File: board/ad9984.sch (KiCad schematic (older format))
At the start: 29 parts, among them P401 AD9984 I2C, U401 AD9984

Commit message: Use smaller testpoint pad
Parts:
- TP401, TP402, TP403, TP404: footprint SMD_Packages:1Pin -> 2MM-TESTPOINT:2MM-TESTPOINT
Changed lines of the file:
@@
 F 0 "TP402" V 6200 5300 60  0000 C CNN
 F 1 "TESTPOINT" H 6150 5300 60  0001 C CNN
-F 2 "SMD_Packages:1Pin" H 6150 5350 60  0001 C CNN
+F 2 "2MM-TESTPOINT:2MM-TESTPOINT" H 6150 5350 60  0001 C CNN
 F 3 "" H 6150 5350 60  0000 C CNN
 	1    6150 5350
@@
 F 0 "TP401" V 4300 4600 60  0000 C CNN
 F 1 "TESTPOINT" H 4400 4400 60  0001 C CNN
-F 2 "SMD_Packages:1Pin" H 4400 4450 60  0001 C CNN
+F 2 "2MM-TESTPOINT:2MM-TESTPOINT" H 4400 4450 60  0001 C CNN
 F 3 "" H 4400 4450 60  0000 C CNN
 	1    4400 4450
@@
 F 0 "TP404" V 6850 1900 60  0000 C CNN
 F 1 "TESTPOINT" H 6950 1700 60  0001 C CNN
-F 2 "SMD_Packages:1Pin" H 6950 1750 60  0001 C CNN
+F 2 "2MM-TESTPOINT:2MM-TESTPOINT" H 6950 1750 60  0001 C CNN
 F 3 "" H 6950 1750 60  0000 C CNN
 	1    6950 1750
@@
 F 0 "TP403" V 6950 1900 60  0000 C CNN
 F 1 "TESTPOINT" H 6850 1700 60  0001 C CNN
-F 2 "SMD_Packages:1Pin" H 6850 1750 60  0001 C CNN
+F 2 "2MM-TESTPOINT:2MM-TESTPOINT" H 6850 1750 60  0001 C CNN
 F 3 "" H 6850 1750 60  0000 C CNN
 	1    6850 1750

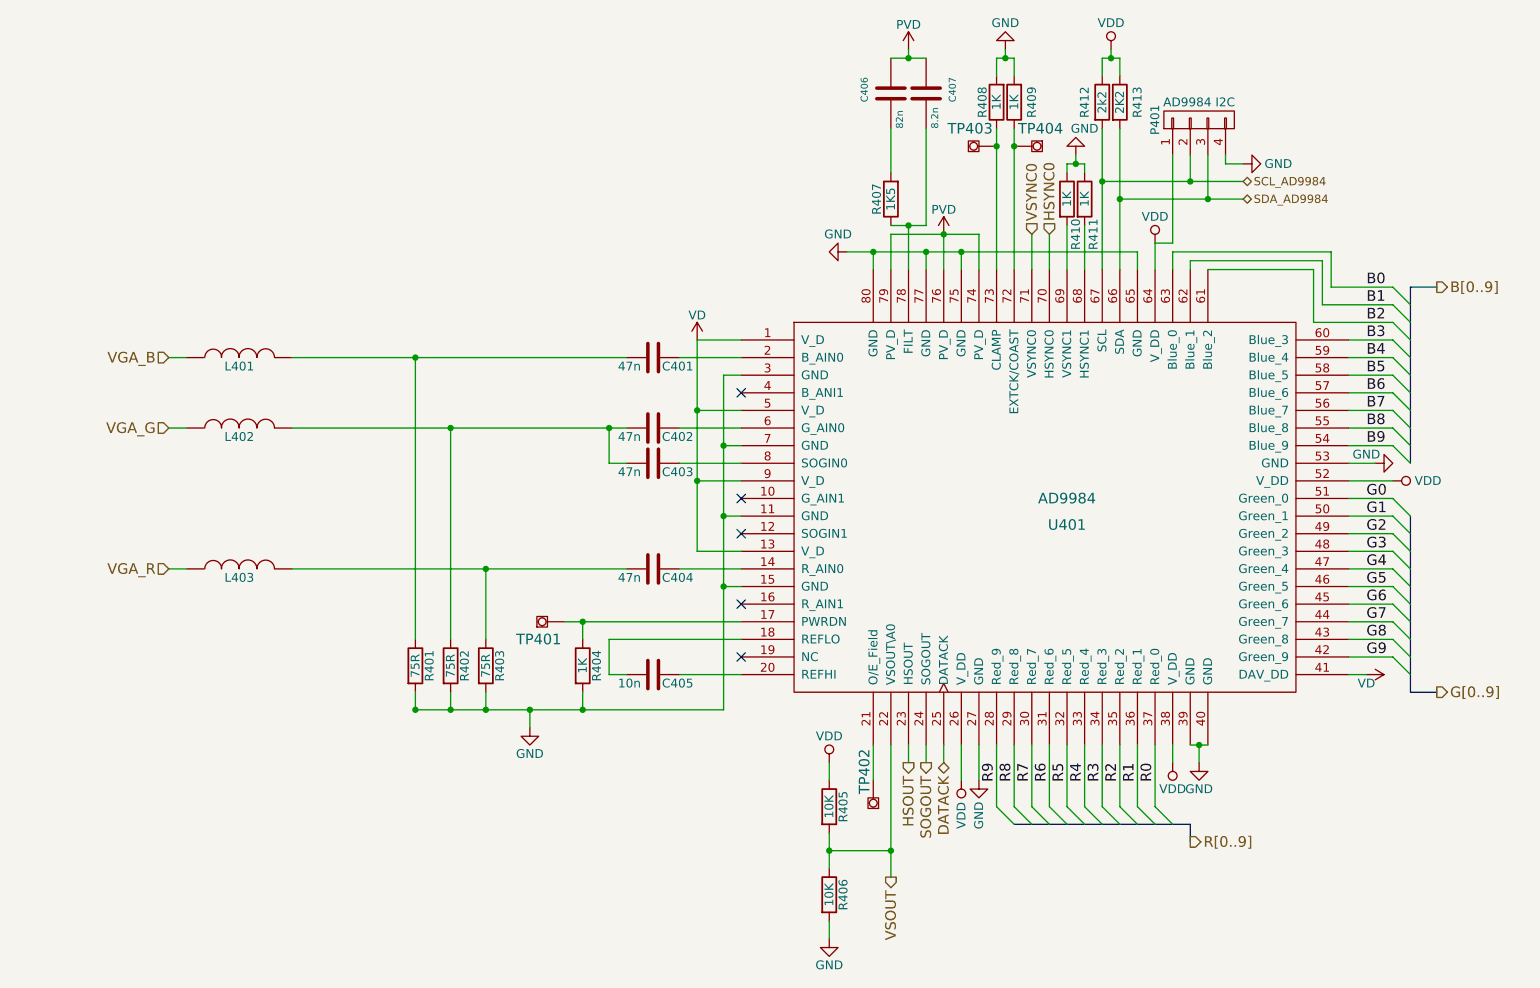
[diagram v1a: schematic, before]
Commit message: Revert "Remove component input to allow design to fit on smaller and much cheaper board"
This reverts commit 3f82e6bce0114ba152d89a6e304191ec714e8d54.
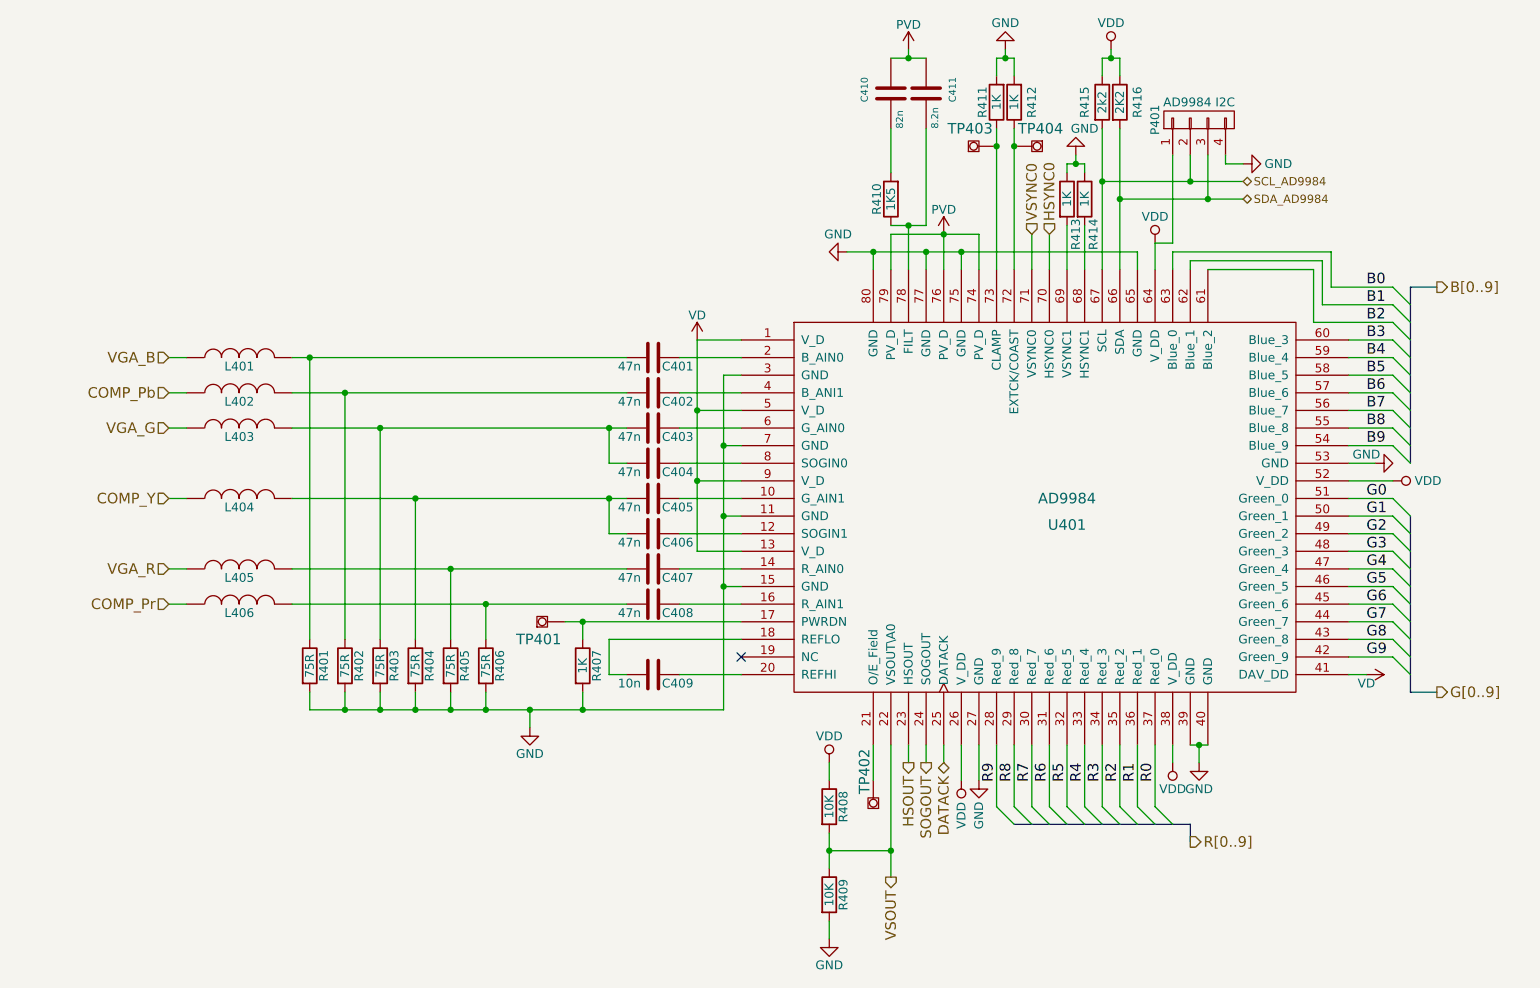
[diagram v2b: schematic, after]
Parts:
- added C402, C405, C406, C408: 47n, Resistors_SMD:R_0805_HandSoldering, symbol C
- added L402, L404, L406: FERRITE, Resistors_SMD:R_0805_HandSoldering, symbol INDUCTOR
- added R401, R402, R403: 75R, Resistors_SMD:R_0805_HandSoldering, symbol R
- renumbered C402 to C403, C403 to C404, C404 to C407, C405 to C409, C406 to C410, C407 to C411, L402 to L403, L403 to L405, R401 to R404, R402 to R405, R403 to R406, R404 to R407, R405 to R408, R406 to R409, R407 to R410, R408 to R411, R409 to R412, R410 to R413, R411 to R414, R412 to R415, R413 to R416
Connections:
- net GND: now also R401.2, R402.2, R403.2
- net at U401.10 (G_AIN1): now also C405.1
- net at U401.12 (SOGIN1): now also C406.1
- net at U401.16 (R_AIN1): now also C408.1
- net at U401.4 (B_ANI1): now also C402.1
- net at C401.2, L401.2: now also R401.1; no longer R404.1
- net at C403.2, C404.2, L403.2: now also R403.1; no longer R405.1
- net at C407.2, L405.2: now also R405.1; no longer R406.1
- new net: C405.2, C406.2, L404.2, R404.1
- new net: C408.2, L406.2, R406.1
- new net: C402.2, L402.2, R402.1
- new net COMP_Pb: L402.1
- new net COMP_Pr: L406.1
- new net COMP_Y: L404.1
- no-connect marks 5 -> 1

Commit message: Adding an analog ground.
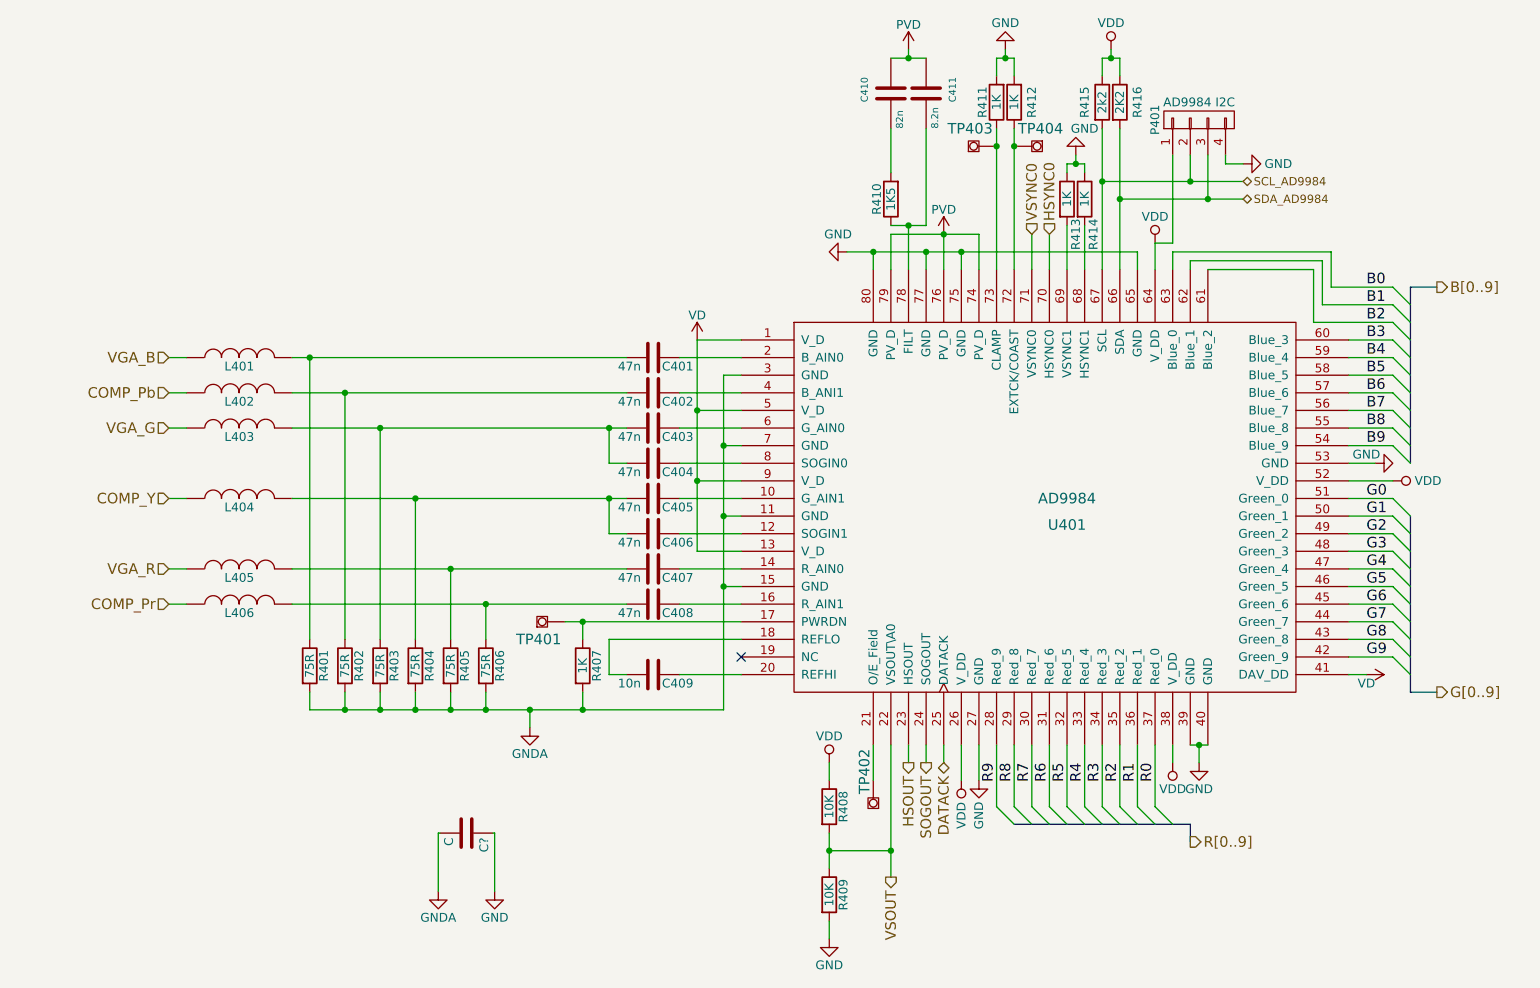
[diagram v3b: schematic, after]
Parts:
- added C?: C, symbol C
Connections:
- net GND: now also C?.1; no longer R401.2, R402.2, R403.2, R404.2, R405.2, R406.2, R407.2, U401.11 (GND), U401.15 (GND), U401.3 (GND), U401.7 (GND)
- new net GNDA: C?.2, R401.2, R402.2, R403.2, R404.2, R405.2, R406.2, R407.2, U401.11 (GND), U401.15 (GND), U401.3 (GND), U401.7 (GND)
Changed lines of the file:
@@
 R[0..9]
 $Comp
-L GND #PWR022
+L GNDA #PWR022
 U 1 1 5640DDDC
 P 4200 5050
 F 0 "#PWR022" H 4200 4800 50  0001 C CNN
-F 1 "GND" H 4200 4900 50  0000 C CNN
+F 1 "GNDA" H 4200 4900 50  0000 C CNN
 F 2 "" H 4200 5050 60  0000 C CNN
 F 3 "" H 4200 5050 60  0000 C CNN
@@
 	8750 2550 9100 2550
 Wire Wire Line
-	7450 1650 7450 2450
-Wire Wire Line
-	7550 1650 7550 2450
+	7450 1650 7450 1950
+Wire Wire Line
+	7450 1950 7450 2450
+Wire Wire Line
+	7550 1650 7550 2050
+Wire Wire Line
+	7550 2050 7550 2450
 Wire Wire Line
 	6150 2350 6150 2450
@@
 	6350 5150 6350 5250
 Wire Wire Line
-	6250 5150 6250 5900
+	6250 5150 6250 5750
+Wire Wire Line
+	6250 5750 6250 5900
 Wire Wire Line
 	6750 5150 6750 5350
@@
 	7850 5150 7850 5250
 Wire Wire Line
-	7950 5150 8050 5150
+	7950 5150 8000 5150
+Wire Wire Line
+	8000 5150 8050 5150
 Wire Wire Line
 	8000 5150 8000 5250
@@
 	5300 4250 5400 4250
 Wire Wire Line
-	4400 4450 5400 4450
+	4400 4450 4500 4450
+Wire Wire Line
+	4500 4450 5400 4450
 Wire Wire Line
 	5050 4750 5400 4750
@@
 Connection ~ 4500 4450
 Wire Wire Line
-	2850 3350 4750 3350
+	2850 3350 3350 3350
+Wire Wire Line
+	3350 3350 4650 3350
+Wire Wire Line
+	4650 3350 4750 3350
 Wire Wire Line
 	8850 2850 9100 2850
@@
 	7350 2200 7350 2450
 Wire Wire Line
-	2850 4150 4750 4150
-Wire Wire Line
-	2850 2950 4750 2950
-Wire Bus Line
-	9200 3550 9200 2550
+	2850 4150 3750 4150
+Wire Wire Line
+	3750 4150 4750 4150
+Wire Wire Line
+	2850 2950 2950 2950
+Wire Wire Line
+	2950 2950 4750 2950
+Wire Bus Line
+	9200 3550 9200 3450
+Wire Bus Line
+	9200 3450 9200 3350
+Wire Bus Line
+	9200 3350 9200 3250
+Wire Bus Line
+	9200 3250 9200 3150
+Wire Bus Line
+	9200 3150 9200 3050
+Wire Bus Line
+	9200 3050 9200 2950
+Wire Bus Line
+	9200 2950 9200 2850
+Wire Bus Line
+	9200 2850 9200 2750
+Wire Bus Line
+	9200 2750 9200 2650
+Wire Bus Line
+	9200 2650 9200 2550
 Wire Bus Line
 	9200 2550 9350 2550
 Wire Bus Line
-	9200 3850 9200 4850
+	9200 3850 9200 3950
+Wire Bus Line
+	9200 3950 9200 4050
+Wire Bus Line
+	9200 4050 9200 4150
+Wire Bus Line
+	9200 4150 9200 4250
+Wire Bus Line
+	9200 4250 9200 4350
+Wire Bus Line
+	9200 4350 9200 4450
+Wire Bus Line
+	9200 4450 9200 4550
+Wire Bus Line
+	9200 4550 9200 4650
+Wire Bus Line
+	9200 4650 9200 4750
+Wire Bus Line
+	9200 4750 9200 4850
 Wire Bus Line
 	9200 4850 9350 4850
 Wire Bus Line
-	6950 5600 7950 5600
+	6950 5600 7050 5600
+Wire Bus Line
+	7050 5600 7150 5600
+Wire Bus Line
+	7150 5600 7250 5600
+Wire Bus Line
+	7250 5600 7350 5600
+Wire Bus Line
+	7350 5600 7450 5600
+Wire Bus Line
+	7450 5600 7550 5600
+Wire Bus Line
+	7550 5600 7650 5600
+Wire Bus Line
+	7650 5600 7750 5600
+Wire Bus Line
+	7750 5600 7850 5600
+Wire Bus Line
+	7850 5600 7950 5600
 Wire Bus Line
 	7950 5600 7950 5700
 Wire Wire Line
-	2950 4950 5300 4950
+	2950 4950 3150 4950
+Wire Wire Line
+	3150 4950 3350 4950
+Wire Wire Line
+	3350 4950 3550 4950
+Wire Wire Line
+	3550 4950 3750 4950
+Wire Wire Line
+	3750 4950 3950 4950
+Wire Wire Line
+	3950 4950 4200 4950
+Wire Wire Line
+	4200 4950 4500 4950
+Wire Wire Line
+	4500 4950 5300 4950
 Wire Wire Line
 	3350 4950 3350 4850
@@
 $EndComp
 Wire Wire Line
-	5150 2850 5150 4050
+	5150 2850 5150 3250
+Wire Wire Line
+	5150 3250 5150 3650
+Wire Wire Line
+	5150 3650 5150 4050
 Connection ~ 5150 3250
 Connection ~ 5150 3650
@@
 $EndComp
 Wire Wire Line
-	5900 5650 5900 5850
+	5900 5650 5900 5750
+Wire Wire Line
+	5900 5750 5900 5850
 Wire Wire Line
 	5900 5350 5900 5250
@@
 $EndComp
 Wire Wire Line
-	5300 4950 5300 3050
+	5300 4950 5300 4250
+Wire Wire Line
+	5300 4250 5300 3850
+Wire Wire Line
+	5300 3850 5300 3450
+Wire Wire Line
+	5300 3450 5300 3050
 Wire Wire Line
 	3550 4850 3550 4950
@@
 $EndComp
 Wire Wire Line
-	6250 2250 6750 2250
+	6250 2250 6550 2250
+Wire Wire Line
+	6550 2250 6750 2250
 Connection ~ 6550 2250
 Wire Wire Line
-	6000 2350 7650 2350
+	6000 2350 6150 2350
+Wire Wire Line
+	6150 2350 6450 2350
+Wire Wire Line
+	6450 2350 6650 2350
+Wire Wire Line
+	6650 2350 7650 2350
 Connection ~ 6450 2350
 Connection ~ 6650 2350
@@
 SCL_AD9984
 Wire Wire Line
-	7450 1950 8250 1950
-Wire Wire Line
-	7550 2050 8250 2050
+	7450 1950 7950 1950
+Wire Wire Line
+	7950 1950 8250 1950
+Wire Wire Line
+	7550 2050 8050 2050
+Wire Wire Line
+	8050 2050 8250 2050
 Connection ~ 7550 2050
 Connection ~ 7450 1950
@@
 	7450 1350 7450 1250
 Wire Wire Line
-	7450 1250 7550 1250
+	7450 1250 7500 1250
+Wire Wire Line
+	7500 1250 7550 1250
 Wire Wire Line
 	7500 1250 7500 1200
@@
 	6850 1350 6850 1250
 Wire Wire Line
-	6850 1250 6950 1250
+	6850 1250 6900 1250
+Wire Wire Line
+	6900 1250 6950 1250
 Wire Wire Line
 	6900 1250 6900 1200
@@
 Connection ~ 6900 1250
 Wire Wire Line
-	6850 1650 6850 2450
-Wire Wire Line
-	6950 1650 6950 2450
+	6850 1650 6850 1750
+Wire Wire Line
+	6850 1750 6850 2450
+Wire Wire Line
+	6950 1650 6950 1750
+Wire Wire Line
+	6950 1750 6950 2450
 $Comp
 L R R410
@@
 	6350 2450 6350 2200
 Wire Wire Line
-	6450 2200 6250 2200
+	6450 2200 6350 2200
+Wire Wire Line
+	6350 2200 6250 2200
 Wire Wire Line
 	6450 1650 6450 2200
@@
 	6250 1650 6250 1900
 Wire Wire Line
-	6250 1250 6450 1250
+	6250 1250 6350 1250
+Wire Wire Line
+	6350 1250 6450 1250
 Wire Wire Line
 	6350 1250 6350 1200
@@
 	7250 1900 7250 1850
 Wire Wire Line
-	7250 1850 7350 1850
+	7250 1850 7300 1850
+Wire Wire Line
+	7300 1850 7350 1850
 Wire Wire Line
 	7300 1850 7300 1800
@@
 	2150 3150 2250 3150
 Wire Wire Line
-	2850 3150 4750 3150
+	2850 3150 3150 3150
+Wire Wire Line
+	3150 3150 4750 3150
 Wire Wire Line
 	4750 3550 4650 3550
@@
 	2150 3750 2250 3750
 Wire Wire Line
-	2850 3750 4750 3750
+	2850 3750 3550 3750
+Wire Wire Line
+	3550 3750 4650 3750
+Wire Wire Line
+	4650 3750 4750 3750
 Wire Wire Line
 	4750 3950 4650 3950
@@
 	2150 4350 2250 4350
 Wire Wire Line
-	2850 4350 4750 4350
+	2850 4350 3950 4350
+Wire Wire Line
+	3950 4350 4750 4350
 Wire Wire Line
 	3950 4850 3950 4950
@@
 	8050 1800 8050 2050
 Connection ~ 8050 2050
+$Comp
+L GNDA #PWR?
+U 1 1 57976F35
+P 3680 5980
+F 0 "#PWR?" H 3680 5730 50  0001 C CNN
+F 1 "GNDA" H 3680 5830 50  0000 C CNN
+F 2 "" H 3680 5980 60  0000 C CNN
+F 3 "" H 3680 5980 60  0000 C CNN
+	1    3680 5980
+	1    0    0    -1
+$EndComp
+$Comp
+L GND #PWR?
+U 1 1 57976FB5
+P 4000 5980
+F 0 "#PWR?" H 4000 5730 50  0001 C CNN
+F 1 "GND" H 4000 5830 50  0000 C CNN
+F 2 "" H 4000 5980 60  0000 C CNN
+F 3 "" H 4000 5980 60  0000 C CNN
+	1    4000 5980
+	1    0    0    -1
+$EndComp
+$Comp
+L C C?
+U 1 1 5797716F
+P 3840 5650
+F 0 "C?" H 3865 5750 50  0000 L CNN
+F 1 "C" H 3865 5550 50  0000 L CNN
+F 2 "" H 3878 5500 50  0000 C CNN
+F 3 "" H 3840 5650 50  0000 C CNN
+	1    3840 5650
+	0    1    1    0
+$EndComp
+Wire Wire Line
+	3680 5980 3680 5650
+Wire Wire Line
+	3680 5650 3690 5650
+Wire Wire Line
+	4000 5980 4000 5650
+Wire Wire Line
+	4000 5650 3990 5650
 $EndSCHEMATC

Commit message: Small fixes to power supplies.
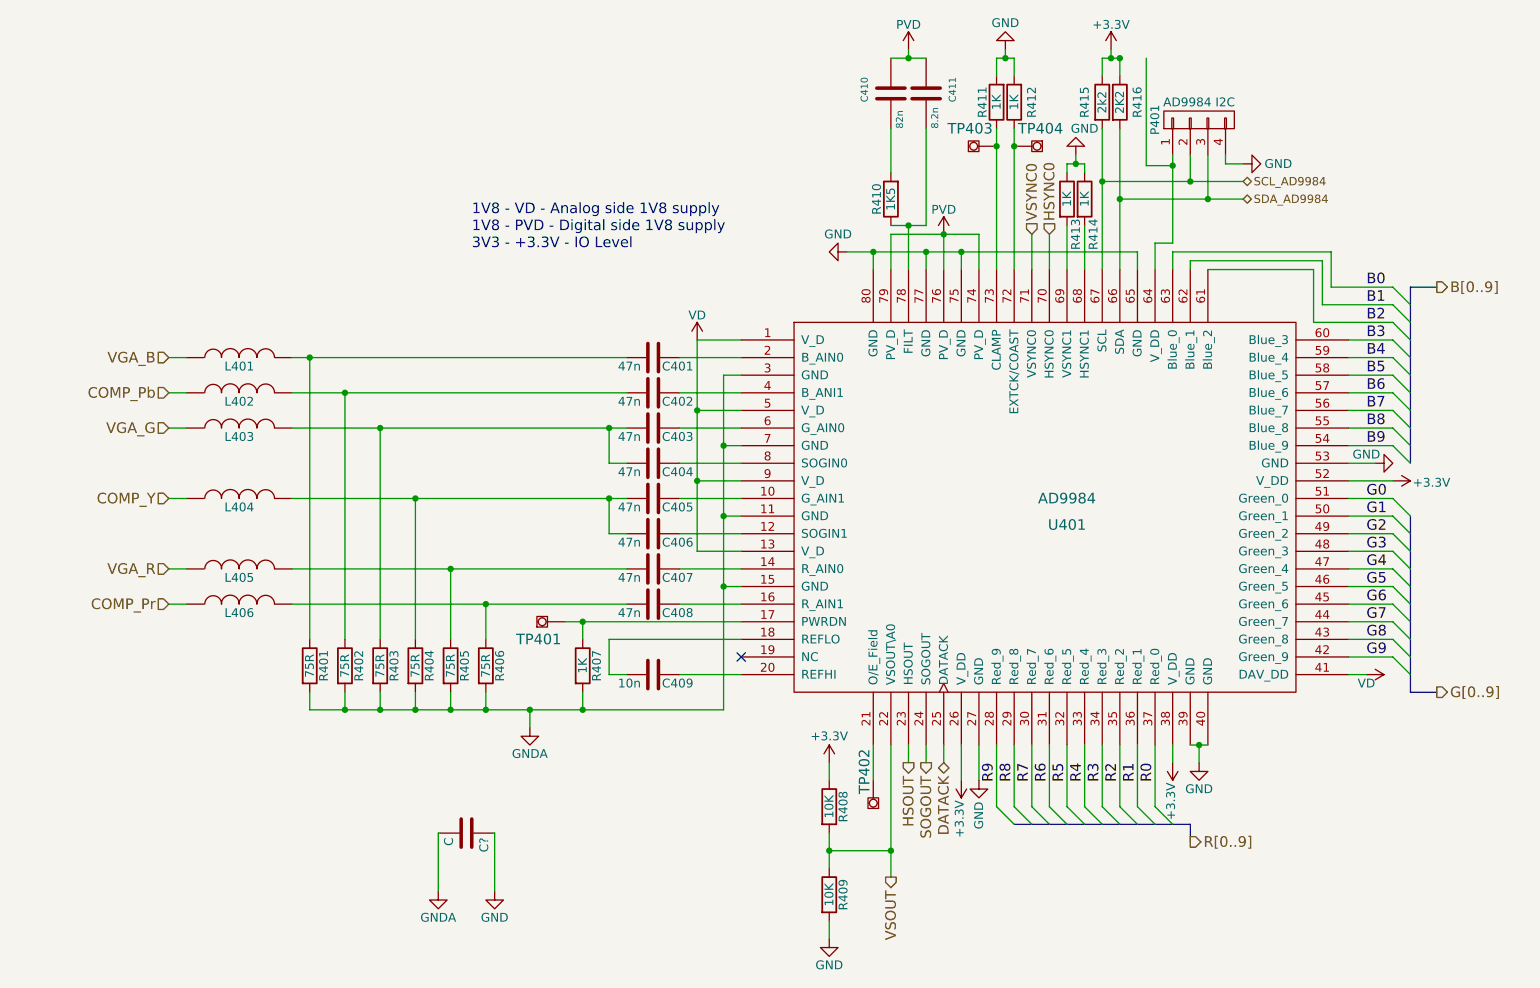
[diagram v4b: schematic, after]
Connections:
- net VDD renamed +3V3
- net +3V3: no longer P401.1 (P1), U401.64 (V_DD)
- new net: P401.1 (P1), U401.64 (V_DD)
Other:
- note added: "1V8 - VD - Analog side 1V8 supply\n1V8 - PVD - Digital side 1V8 supply\n3V3 - +3.3V - IO Level"
